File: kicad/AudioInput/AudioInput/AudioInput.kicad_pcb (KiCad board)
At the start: 2 copper layers, 48.9 x 55.5 mm, 61 parts, among them J1 EXPAN2, J2 EXPAN1, J3 INT INPUT, K1 G6K-2, Q1 BS250, Q2 2N7000, Q3 BS250, U1 MCP4651, U2 LM324, U3 CD4052B

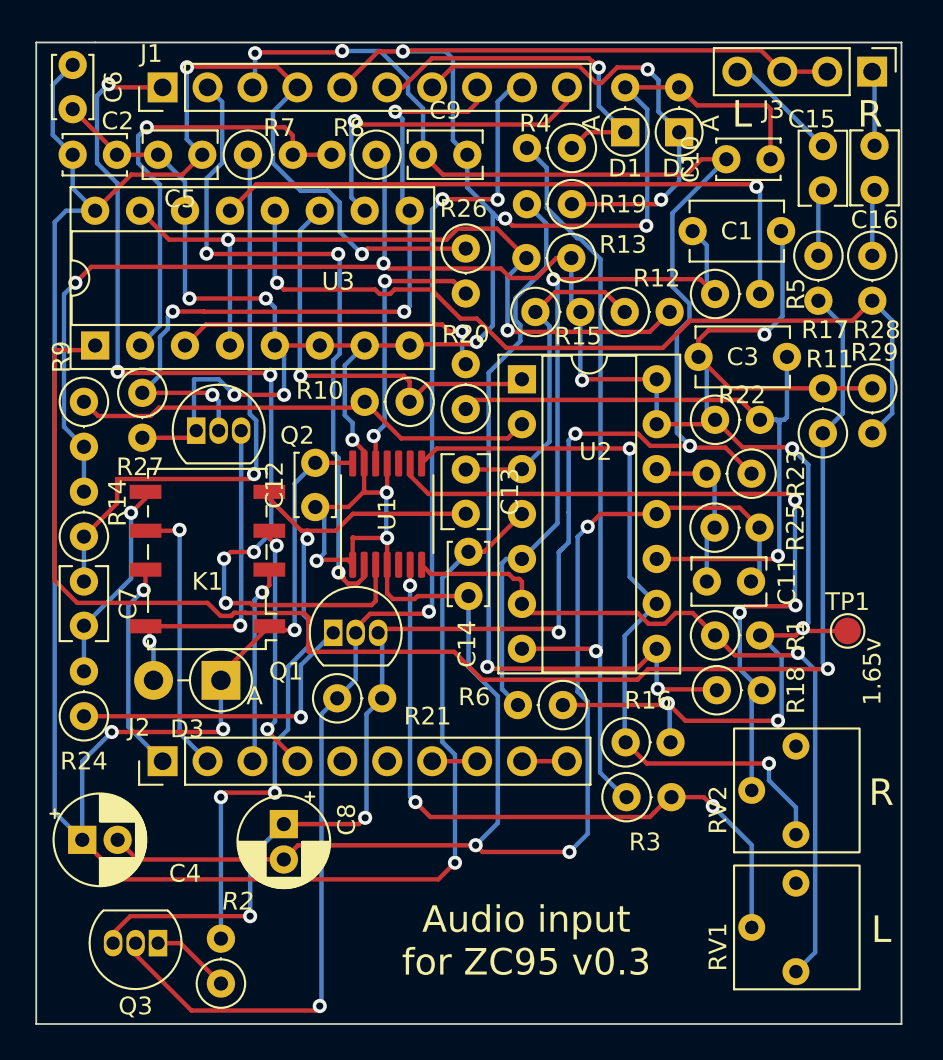
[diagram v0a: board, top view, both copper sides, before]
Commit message: Audio input board redesign for SMT (#133)
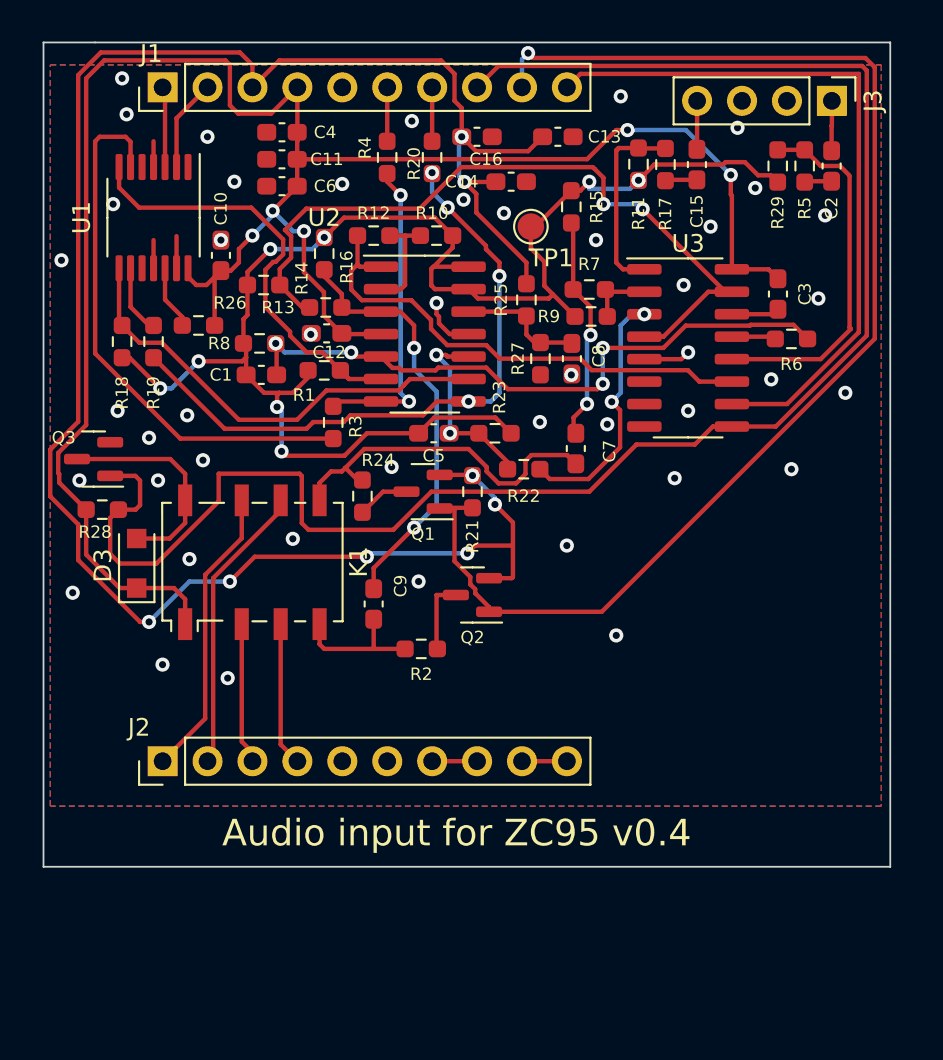
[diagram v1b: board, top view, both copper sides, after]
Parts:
- removed D1, D2: 3.3v, Diode_THT:D_DO-35_SOD27_P2.54mm_Vertical_AnodeUp
- removed RV1, RV2: 50k, Library:3362P-1-503
- C1: value 3nF -> 3.3nF; footprint Capacitor_THT:C_Disc_D5.1mm_W3.2mm_P5.00mm -> Capacitor_SMD:C_0603_1608Metric_Pad1.08x0.95mm_HandSolder
- C10, C12, C6: footprint Capacitor_THT:C_Disc_D3.4mm_W2.1mm_P2.50mm -> Capacitor_SMD:C_0603_1608Metric_Pad1.08x0.95mm_HandSolder
- C11, C15, C7, C9: footprint Capacitor_THT:C_Rect_L4.0mm_W2.5mm_P2.50mm -> Capacitor_SMD:C_0603_1608Metric_Pad1.08x0.95mm_HandSolder
- C13: value 1uF -> 10uF; footprint Capacitor_THT:C_Rect_L4.0mm_W2.5mm_P2.50mm -> Capacitor_SMD:C_0603_1608Metric_Pad1.08x0.95mm_HandSolder
- C14, C2: value 100nF -> 1uF; footprint Capacitor_THT:C_Disc_D3.4mm_W2.1mm_P2.50mm -> Capacitor_SMD:C_0603_1608Metric_Pad1.08x0.95mm_HandSolder
- C16: value 1uF -> 100nF; footprint Capacitor_THT:C_Rect_L4.0mm_W2.5mm_P2.50mm -> Capacitor_SMD:C_0603_1608Metric_Pad1.08x0.95mm_HandSolder
- C3: value 3nF -> 100nF; footprint Capacitor_THT:C_Disc_D5.1mm_W3.2mm_P5.00mm -> Capacitor_SMD:C_0603_1608Metric_Pad1.08x0.95mm_HandSolder
- C4: footprint Capacitor_THT:CP_Radial_D5.0mm_P2.00mm -> Capacitor_SMD:C_0603_1608Metric_Pad1.08x0.95mm_HandSolder
- C5: value 1uF -> 3.3nF; footprint Capacitor_THT:C_Rect_L4.0mm_W2.5mm_P2.50mm -> Capacitor_SMD:C_0603_1608Metric_Pad1.08x0.95mm_HandSolder
- C8: value 10uF -> 1uF; footprint Capacitor_THT:CP_Radial_D5.0mm_P2.00mm -> Capacitor_SMD:C_0603_1608Metric_Pad1.08x0.95mm_HandSolder
- D3: value 1N4004 -> SM4007PL; footprint Diode_THT:D_DO-41_SOD81_P3.81mm_Vertical_AnodeUp -> Diode_SMD:D_SOD-123F
- Q1: value BS250 -> AO3401A; footprint Package_TO_SOT_THT:TO-92_Inline -> Package_TO_SOT_SMD:SOT-23
- Q2: value 2N7000 -> AO3401A; footprint Package_TO_SOT_THT:TO-92_Inline -> Package_TO_SOT_SMD:SOT-23
- Q3: value BS250 -> AO3400A; footprint Package_TO_SOT_THT:TO-92_Inline -> Package_TO_SOT_SMD:SOT-23
- R1, R11, R12, R15, R17, R21, R23, R25, R26, R27, R28, R29, R3, R4, R7: footprint Resistor_THT:R_Axial_DIN0207_L6.3mm_D2.5mm_P2.54mm_Vertical -> Resistor_SMD:R_0603_1608Metric_Pad0.98x0.95mm_HandSolder
- R10: value 100k -> 4k7; footprint Resistor_THT:R_Axial_DIN0207_L6.3mm_D2.5mm_P2.54mm_Vertical -> Resistor_SMD:R_0603_1608Metric_Pad0.98x0.95mm_HandSolder
- R13, R8: value 150k -> 100k; footprint Resistor_THT:R_Axial_DIN0207_L6.3mm_D2.5mm_P2.54mm_Vertical -> Resistor_SMD:R_0603_1608Metric_Pad0.98x0.95mm_HandSolder
- R14: value 100k -> 150k; footprint Resistor_THT:R_Axial_DIN0207_L6.3mm_D2.5mm_P2.54mm_Vertical -> Resistor_SMD:R_0603_1608Metric_Pad0.98x0.95mm_HandSolder
- R16: value 4k7 -> 100k; footprint Resistor_THT:R_Axial_DIN0207_L6.3mm_D2.5mm_P2.54mm_Vertical -> Resistor_SMD:R_0603_1608Metric_Pad0.98x0.95mm_HandSolder
- R18: value 10k -> 4k7; footprint Resistor_THT:R_Axial_DIN0207_L6.3mm_D2.5mm_P2.54mm_Vertical -> Resistor_SMD:R_0603_1608Metric_Pad0.98x0.95mm_HandSolder
- R19: value 1k -> 10k; footprint Resistor_THT:R_Axial_DIN0207_L6.3mm_D2.5mm_P2.54mm_Vertical -> Resistor_SMD:R_0603_1608Metric_Pad0.98x0.95mm_HandSolder
- R2, R24: value 2k7 -> 2k2; footprint Resistor_THT:R_Axial_DIN0207_L6.3mm_D2.5mm_P2.54mm_Vertical -> Resistor_SMD:R_0603_1608Metric_Pad0.98x0.95mm_HandSolder
- R20: value 10k -> 1k; footprint Resistor_THT:R_Axial_DIN0207_L6.3mm_D2.5mm_P2.54mm_Vertical -> Resistor_SMD:R_0603_1608Metric_Pad0.98x0.95mm_HandSolder
- R22, R6: value 100k -> 10k; footprint Resistor_THT:R_Axial_DIN0207_L6.3mm_D2.5mm_P2.54mm_Vertical -> Resistor_SMD:R_0603_1608Metric_Pad0.98x0.95mm_HandSolder
- R5: value 10k -> 100k; footprint Resistor_THT:R_Axial_DIN0207_L6.3mm_D2.5mm_P2.54mm_Vertical -> Resistor_SMD:R_0603_1608Metric_Pad0.98x0.95mm_HandSolder
- R9: value 10k -> 150k; footprint Resistor_THT:R_Axial_DIN0207_L6.3mm_D2.5mm_P2.54mm_Vertical -> Resistor_SMD:R_0603_1608Metric_Pad0.98x0.95mm_HandSolder
- U2: footprint Package_DIP:DIP-14_W7.62mm_Socket -> Package_SO:SOIC-14_3.9x8.7mm_P1.27mm
- U3: footprint Package_DIP:DIP-16_W7.62mm_Socket -> Package_SO:SOIC-16_3.9x9.9mm_P1.27mm
- moved R28 45.8 mm to (132.5, 89.9), turned to 0 degrees
- moved C4 41.6 mm to (142.6, 68.6), turned to 180 degrees
- moved C2 40.4 mm to (173.7, 70.5), turned to -90 degrees
- moved R18 39.0 mm to (133.6, 80.4), turned to -90 degrees
- moved C11 35.7 mm to (142.6, 70.1), turned to 0 degrees
- moved U3 33.5 mm to (165.6, 80.8), turned to 0 degrees
- moved R16 32.5 mm to (145.0, 75.4), turned to -90 degrees
- moved C8 30.9 mm to (159.0, 81.4), turned to 90 degrees
- moved C10 29.1 mm to (139.2, 75.5), turned to 90 degrees
- moved R9 29.1 mm to (160.1, 79.0), turned to 0 degrees
- moved TP1 29.0 mm to (156.7, 73.9)
- moved C7 28.8 mm to (159.3, 86.5)
- moved Q3 27.6 mm to (132.0, 87.1)
- moved R3 26.9 mm to (145.5, 85.0), turned to -90 degrees
- moved R1 26.7 mm to (145.0, 82.0), turned to 180 degrees
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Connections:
- C10 pad 1: 3v3 -> 5v
- C11 pad 2: Net-(C11-Pad2) -> 5v
- C12 pad 1: GND -> 5v
- C12 pad 2: 5v -> GND
- C13 pad 1: AUDIO_IN_L -> 3v3
- C13 pad 2: Net-(C13-Pad2) -> GND
- C14 pad 2: 5v -> 3v3
- C16 pad 1: Net-(C16-Pad1) -> 3v3
- C16 pad 2: Net-(C16-Pad2) -> GND
- C2 pad 1: GND -> Net-(J3-Pad1)
- C2 pad 2: 5v -> Net-(C2-Pad2)
- C3 pad 1: Net-(C3-Pad1) -> GND
- C3 pad 2: 1.65v -> 5v
- C5 pad 1: 5v -> Net-(U2-Pad10)
- C5 pad 2: GND -> 1.65v
- C8 pad 1: 3v3 -> GND
- C8 pad 2: GND -> Net-(U2-Pad12)
- C9 pad 1: 3v3 -> AUDIO_IN_L
- C9 pad 2: GND -> Net-(K1-Pad4)
- D3 pad 2: Net-(K1-Pad8) -> Net-(D3-Pad2)
- J3 pad 1: Net-(C16-Pad1) -> Net-(J3-Pad1)
- K1 pad 4: Net-(C13-Pad2) -> Net-(K1-Pad4)
- K1 pad 8: Net-(K1-Pad8) -> Net-(D3-Pad2)
- Q1 pad 1: Net-(Q1-Pad1) -> MIC_PWR_DIS
- Q1 pad 2: MIC_PWR_DIS -> 3v3
- Q1 pad 3: 3v3 -> Net-(R24-Pad1)
- Q2 pad 1: GND -> MIC_PWR_DIS
- Q2 pad 2: AUDIO_EN -> 3v3
- Q2 pad 3: Net-(K1-Pad8) -> Net-(R2-Pad1)
- Q3 pad 1: Net-(Q3-Pad1) -> AUDIO_EN
- Q3 pad 2: MIC_PWR_DIS -> GND
- Q3 pad 3: 3v3 -> Net-(D3-Pad2)
- R10 pad 1: MIC_PREAMP_OUT -> Net-(U2-Pad2)
- R10 pad 2: Net-(R10-Pad2) -> 1.65v
- R12 pad 1: AUDIO_IN_L -> Net-(U2-Pad2)
- R12 pad 2: Net-(R12-Pad2) -> MIC_PREAMP_OUT
- R13 pad 1: 1.65v -> AUDIO_IN_L
- R13 pad 2: Net-(R12-Pad2) -> Net-(U3-Pad15)
- R14 pad 1: AUDIO_IN_R -> 1.65v
- R14 pad 2: 1.65v -> Net-(U3-Pad15)
- R15 pad 1: AUDIO_IN_L -> 1.65v
- R15 pad 2: 1.65v -> AUDIO_IN_R
- R16 pad 1: Net-(R16-Pad1) -> 1.65v
- R16 pad 2: 1.65v -> AUDIO_IN_L
- R18 pad 1: Net-(R18-Pad1) -> Net-(U1-Pad8)
- R18 pad 2: Net-(R18-Pad2) -> 1.65v
- R19 pad 1: ADC2 -> Net-(U2-Pad8)
- R19 pad 2: Net-(R18-Pad1) -> Net-(U1-Pad9)
- R2 pad 1: Net-(Q3-Pad1) -> Net-(R2-Pad1)
- R2 pad 2: Net-(C13-Pad2) -> Net-(K1-Pad4)
- R20 pad 1: Net-(C3-Pad1) -> ADC2
- R20 pad 2: AUDIO_R -> Net-(U2-Pad8)
- R22 pad 1: 1.65v -> Net-(U2-Pad10)
- R22 pad 2: Net-(C3-Pad1) -> AUDIO_R
- R23 pad 1: 3v3 -> 1.65v
- R23 pad 2: Net-(C11-Pad2) -> Net-(U2-Pad10)
- R24 pad 1: Net-(Q1-Pad1) -> Net-(R24-Pad1)
- R25 pad 1: Net-(C11-Pad2) -> Net-(U2-Pad12)
- R25 pad 2: GND -> 3v3
- R27 pad 1: AUDIO_EN -> Net-(U2-Pad12)
- R28 pad 1: Net-(C16-Pad2) -> 5v
- R28 pad 2: INT_INPUT_R -> AUDIO_EN
- R5 pad 1: Net-(C1-Pad1) -> Net-(C2-Pad2)
- R5 pad 2: AUDIO_L -> INT_INPUT_R
- R6 pad 1: 1.65v -> Net-(C1-Pad1)
- R6 pad 2: Net-(C1-Pad1) -> AUDIO_L
- R7 pad 2: Net-(R7-Pad2) -> Net-(R9-Pad2)
- R8 pad 2: Net-(R7-Pad2) -> Net-(C1-Pad1)
- R9 pad 1: Net-(R10-Pad2) -> 1.65v
- R9 pad 2: 1.65v -> Net-(R9-Pad2)
- U1 pad 8: Net-(R16-Pad1) -> Net-(U1-Pad8)
- U1 pad 9: Net-(R18-Pad2) -> Net-(U1-Pad9)
- U2 pad 10: Net-(C3-Pad1) -> Net-(U2-Pad10)
- U2 pad 12: Net-(C11-Pad2) -> Net-(U2-Pad12)
- U2 pad 2: Net-(R10-Pad2) -> Net-(U2-Pad2)
- U2 pad 8: Net-(R18-Pad1) -> Net-(U2-Pad8)
- U2 pad 9: Net-(R16-Pad1) -> Net-(U1-Pad8)
- U3 pad 15: Net-(R12-Pad2) -> Net-(U3-Pad15)
- U3 pad 2: Net-(R7-Pad2) -> Net-(R9-Pad2)
- U3 pad 4: Net-(R12-Pad2) -> Net-(U3-Pad15)
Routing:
- net GND: track 236.1 -> 13.4 mm, vias 15 -> 45
- net INT_INPUT_L: track 84.9 -> 11.1 mm, vias 1 -> 0
- net AUDIO_EN: track 42.1 -> 98.3 mm, vias 4 -> 0
- net SDA: track 54.6 -> 4.56 mm, vias 6 -> 0
- net 5v: track 164.8 -> 116.0 mm, vias 6 -> 5
- net 1.65v: track 132.6 -> 85.6 mm
- net Net-(R18-Pad1): track 43.8 -> 0.00 mm, vias 2 -> 0
- net Net-(R18-Pad2): track 43.7 -> 0.00 mm, vias 3 -> 0
- net Net-(R12-Pad2): track 43.7 -> 0.00 mm, vias 2 -> 0
- net Net-(R16-Pad1): track 43.4 -> 0.00 mm, vias 2 -> 0
- net Net-(U3-Pad15): track 0.00 -> 42.3 mm, vias 0 -> 2
- net Net-(C13-Pad2): track 39.6 -> 0.00 mm, vias 3 -> 0
- net Net-(C3-Pad1): track 38.0 -> 0.00 mm, vias 1 -> 0
- net Net-(U2-Pad8): track 0.00 -> 36.1 mm, vias 0 -> 4
- net AUDIO_L: track 36.6 -> 2.51 mm, vias 1 -> 0
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- added copper zone on B.Cu, net GND
- added copper zone on F.Cu, net GND
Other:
- board size 48.9 x 55.5 mm -> 47.9 x 46.6 mm
- board text added: "Audio input for ZC95 v0.4"
- board text removed: "1.65v"
- board text removed: "Audio input for ZC95 v0.3"
- board text removed: "L"
- board text removed: "R"
